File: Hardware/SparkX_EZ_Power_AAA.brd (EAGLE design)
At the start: 10.7 x 40.6 mm, 43 parts, among them J3 AVR_SPI_PROG_3X2TESTPOINTS, U1 ATTINY43_QFN20, U2 TPS61200

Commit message: Post-review updates
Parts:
- added RXD, TXD: TEST-POINT3X4, SparkFun-Connectors:PAD.03X.04
- added U$4: (no value), output:#TXD#0
- added U$9: (no value), output:#RXD#0
- C1: device SparkFun-Capacitors:0603 -> SparkFun-Capacitors:0402-TIGHT
- C2, C4, C6: device SparkFun-Capacitors:0402 -> SparkFun-Capacitors:0402-TIGHT
- L2: device SparkFun:CDRH2D09 -> SparkFun-Coils:1008(2520)
- R1, R2, R3: device SparkFun-Resistors:0603 -> New-Parts_SparkFun-Resistors:0402-TIGHT
- U2: device SparkFun:QFN-10_PAD -> SparkFun-IC-Power:QFN-10_PAD
- moved U$5 5.12 mm to (8.95, 34.5)
- moved U$2 3.43 mm to (9.84, 11.7)
- moved R1 3.23 mm to (2.35, 8.19)
- moved VIN 2.84 mm to (7.62, 35.6)
- moved R2 2.29 mm to (8.83, 9.78)
- moved U$20 1.27 mm to (5.33, 27.9)
- moved U$3 0.64 mm to (5.33, 26.0)
- moved L2 0.64 mm to (5.84, 9.78)
- moved R3 0.54 mm to (4.76, 17.0)
- moved C6 0.34 mm to (2.35, 11.4)
- moved C4 0.32 mm to (2.35, 12.5)
- moved C2 0.32 mm to (6.92, 17.5)
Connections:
- new net RXD: RXD.1, U1.16
- new net TXD: TXD.1, U1.15
- net N$1: now also L2.1; no longer L2.P$1
- net VIN: now also L2.2; no longer L2.P$2
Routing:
- net VIN: track 57.7 -> 47.2 mm
- net TXD: track 0.00 -> 8.27 mm, vias 0 -> 1
- net RXD: track 0.00 -> 2.65 mm, vias 0 -> 1
- net 3.3V: track 70.9 -> 71.9 mm
- net UVLO: track 4.30 -> 3.74 mm
- net GND: track 85.3 -> 85.0 mm, vias 44 -> 46
- net FB: track 15.9 -> 15.7 mm, vias 2 -> 3

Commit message: Post-review updates
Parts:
- L2: value 4.7uH, 1.2A -> 4.7μH; device SparkFun-Coils:1008(2520) -> SparkFun-Coils:INDUCTOR_4X4MM
- moved VIN 25.4 mm to (7.62, 10.2)
- moved U$5 24.6 mm to (5.40, 10.2)
- moved R2 6.36 mm to (2.98, 7.27), turned to 0 degrees
- moved U$4 4.76 mm to (3.94, 33.0)
- moved U$9 4.76 mm to (4.00, 30.5)
- moved U$2 2.67 mm to (9.65, 9.02)
- moved LOGO2 1.72 mm to (1.84, 16.7)
- moved L2 0.86 mm to (6.35, 9.08), turned to 90 degrees
- moved R1 0.64 mm to (2.98, 8.26)
- moved C3 0.32 mm to (2.32, 10.1)
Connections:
- net N$1: now also L2.P$1; no longer L2.1
- net VIN: now also L2.P$2; no longer L2.2
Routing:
- net FB: track 15.7 -> 9.68 mm, vias 3 -> 2
- net GND: track 85.0 -> 86.6 mm, vias 46 -> 47
- net VIN: track 47.2 -> 46.2 mm
- net N$1: track 3.09 -> 3.75 mm

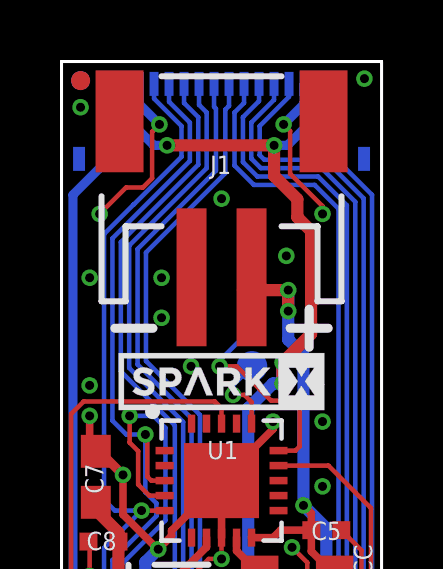
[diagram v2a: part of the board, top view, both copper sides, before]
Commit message: Add VIN Max 5.5V
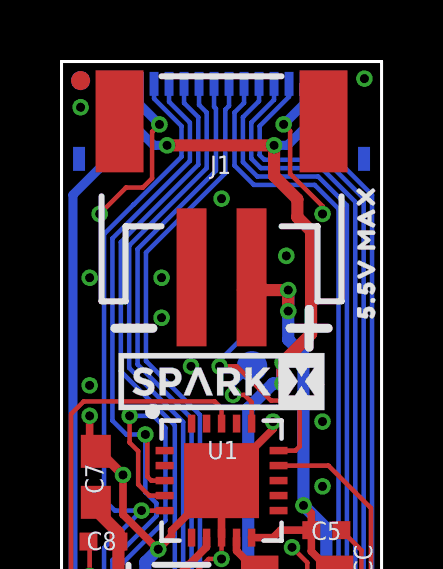
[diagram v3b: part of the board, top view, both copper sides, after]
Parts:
- added U$10: (no value), output:5#5V_MAX0
- U1: device New-Parts_SparkFun-IC-Microcontroller:QFN20_20M1 -> SparkFun-IC-Microcontroller:QFN20_20M1
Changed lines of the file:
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@@
 <element name="PROC_PWR_EN" library="SparkFun-Jumpers" package="SMT-JUMPER_2_NC_TRACE_SILK" package3d_urn="urn:adsk.eagle:package:39281/1" value="JUMPER-SMT_2_NC_TRACE_SILK" x="9.3345" y="3.6195" smashed="yes" rot="MR90"/>
 <element name="3V3_EN" library="SparkFun-Connectors" package="PAD.03X.04" value="TEST-POINT3X4" x="7.62" y="13.97" smashed="yes" rot="MR0"/>
-<element name="U1" library="New-Parts_SparkFun-IC-Microcontroller" package="QFN20_20M1" value="ATTINY43_QFN20" x="5.334" y="26.67" smashed="yes">
+<element name="U1" library="SparkFun-IC-Microcontroller" package="QFN20_20M1" value="ATTINY43_QFN20" x="5.334" y="26.67" smashed="yes">
 <attribute name="DIGIKEY_PART" value="ATTINY43U-MU-ND" x="5.334" y="26.67" size="1.778" layer="27" font="vector" ratio="15" display="off"/>
 <attribute name="MANU_PART" value="ATtiny43U-MU" x="5.334" y="26.67" size="1.778" layer="27" font="vector" ratio="15" display="off"/>
@@
 <element name="U$4" library="output" package="#TXD#0" value="" x="3.937" y="33.02" smashed="yes" rot="MR0"/>
 <element name="U$9" library="output" package="#RXD#0" value="" x="4.0005" y="30.48" smashed="yes" rot="MR0"/>
+<element name="U$10" library="output" package="5#5V_MAX0" value="" x="10.16" y="34.29" smashed="yes" rot="R90"/>
 </elements>
 <signals>

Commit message: Final tweaks
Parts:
- added U$11: (no value), output:MAX0
- U$10: device output:5#5V_MAX0 -> output:5#5V0
- moved U$1 21.7 mm to (9.53, 8.64), turned to 90 degrees
- moved U$2 11.8 mm to (1.46, 17.5)
- moved LOGO2 7.51 mm to (9.33, 16.1), turned to 90 degrees
- moved U$10 4.06 mm to (8.95, 30.4), turned to 0 degrees
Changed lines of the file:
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@@
 <attribute name="PROD_ID" value="" x="5.334" y="2.0955" size="1.778" layer="27" font="vector" ratio="15" rot="R180" display="off"/>
 </element>
-<element name="LOGO2" library="SparkFun-Aesthetics" package="OSHW-LOGO-MINI" value="OSHW-LOGOMINI" x="1.8415" y="16.7005" smashed="yes"/>
-<element name="U$1" library="SparkX" package="SPARKX-SMALL" value="SPARKX-LOGO3" x="5.334" y="29.972" smashed="yes"/>
+<element name="LOGO2" library="SparkFun-Aesthetics" package="OSHW-LOGO-MINI" value="OSHW-LOGOMINI" x="9.3345" y="16.129" smashed="yes" rot="R90"/>
+<element name="U$1" library="SparkX" package="SPARKX-SMALL" value="SPARKX-LOGO3" x="9.525" y="8.636" smashed="yes" rot="R90"/>
 <element name="U$13" library="output" package="#OUT#0" value="" x="5.334" y="4.8895" smashed="yes"/>
 <element name="U$20" library="SparkX" package="SPARKX-SMALL" value="SPARKX-LOGO3" x="5.334" y="27.94" smashed="yes" rot="MR0"/>
@@
 <attribute name="PROD_ID" value="RES-15093" x="6.9215" y="16.4465" size="1.778" layer="27" ratio="15" rot="R180" display="off"/>
 </element>
-<element name="U$2" library="output" package="EZ_POWER_AAA0" value="" x="9.652" y="9.017" smashed="yes" rot="R90"/>
+<element name="U$2" library="output" package="EZ_POWER_AAA0" value="" x="1.4605" y="17.4625" smashed="yes" rot="R90"/>
 <element name="U$3" library="output" package="EZ_POWER_AAA0" value="" x="5.334" y="26.035" smashed="yes" rot="MR0"/>
 <element name="U2" library="SparkFun-IC-Power" package="QFN-10_PAD" value="TPS61200" x="5.334" y="13.97" smashed="yes">
@@
 <element name="U$4" library="output" package="#TXD#0" value="" x="3.937" y="33.02" smashed="yes" rot="MR0"/>
 <element name="U$9" library="output" package="#RXD#0" value="" x="4.0005" y="30.48" smashed="yes" rot="MR0"/>
-<element name="U$10" library="output" package="5#5V_MAX0" value="" x="10.16" y="34.29" smashed="yes" rot="R90"/>
+<element name="U$10" library="output" package="5#5V0" value="" x="8.9535" y="30.4165" smashed="yes"/>
+<element name="U$11" library="output" package="MAX0" value="" x="8.9535" y="29.464" smashed="yes"/>
 </elements>
 <signals>

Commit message: Gapless production panel
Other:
- board text added: "2-Layer Board 1.6mm Thickness 1oz Copper (Outer layers) HASL Finish"
- board text removed: "2-Layer Board 1.6mm Thickness 1oz Copper (Outer layers) HASL Finish When running the panelizer, add a vertical gap of 0.2" to make the boards easier to separate"
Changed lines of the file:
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@@
 <layer number="23" name="tOrigins" color="15" fill="1" visible="yes" active="yes"/>
 <layer number="24" name="bOrigins" color="15" fill="1" visible="yes" active="yes"/>
-<layer number="25" name="tNames" color="57" fill="1" visible="yes" active="yes"/>
-<layer number="26" name="bNames" color="57" fill="1" visible="yes" active="yes"/>
-<layer number="27" name="tValues" color="7" fill="1" visible="yes" active="yes"/>
-<layer number="28" name="bValues" color="7" fill="1" visible="yes" active="yes"/>
-<layer number="29" name="tStop" color="7" fill="3" visible="yes" active="yes"/>
-<layer number="30" name="bStop" color="7" fill="6" visible="yes" active="yes"/>
-<layer number="31" name="tCream" color="7" fill="4" visible="yes" active="yes"/>
-<layer number="32" name="bCream" color="7" fill="5" visible="yes" active="yes"/>
-<layer number="33" name="tFinish" color="6" fill="3" visible="yes" active="yes"/>
-<layer number="34" name="bFinish" color="6" fill="6" visible="yes" active="yes"/>
-<layer number="35" name="tGlue" color="7" fill="4" visible="yes" active="yes"/>
-<layer number="36" name="bGlue" color="7" fill="5" visible="yes" active="yes"/>
-<layer number="37" name="tTest" color="7" fill="1" visible="yes" active="yes"/>
-<layer number="38" name="bTest" color="7" fill="1" visible="yes" active="yes"/>
-<layer number="39" name="tKeepout" color="4" fill="11" visible="yes" active="yes"/>
-<layer number="40" name="bKeepout" color="1" fill="11" visible="yes" active="yes"/>
-<layer number="41" name="tRestrict" color="4" fill="10" visible="yes" active="yes"/>
-<layer number="42" name="bRestrict" color="1" fill="10" visible="yes" active="yes"/>
-<layer number="43" name="vRestrict" color="2" fill="10" visible="yes" active="yes"/>
-<layer number="44" name="Drills" color="7" fill="1" visible="yes" active="yes"/>
+<layer number="25" name="tNames" color="57" fill="1" visible="no" active="yes"/>
+<layer number="26" name="bNames" color="57" fill="1" visible="no" active="yes"/>
+<layer number="27" name="tValues" color="7" fill="1" visible="no" active="yes"/>
+<layer number="28" name="bValues" color="7" fill="1" visible="no" active="yes"/>
+<layer number="29" name="tStop" color="7" fill="3" visible="no" active="yes"/>
+<layer number="30" name="bStop" color="7" fill="6" visible="no" active="yes"/>
+<layer number="31" name="tCream" color="7" fill="4" visible="no" active="yes"/>
+<layer number="32" name="bCream" color="7" fill="5" visible="no" active="yes"/>
+<layer number="33" name="tFinish" color="6" fill="3" visible="no" active="yes"/>
+<layer number="34" name="bFinish" color="6" fill="6" visible="no" active="yes"/>
+<layer number="35" name="tGlue" color="7" fill="4" visible="no" active="yes"/>
+<layer number="36" name="bGlue" color="7" fill="5" visible="no" active="yes"/>
+<layer number="37" name="tTest" color="7" fill="1" visible="no" active="yes"/>
+<layer number="38" name="bTest" color="7" fill="1" visible="no" active="yes"/>
+<layer number="39" name="tKeepout" color="4" fill="11" visible="no" active="yes"/>
+<layer number="40" name="bKeepout" color="1" fill="11" visible="no" active="yes"/>
+<layer number="41" name="tRestrict" color="4" fill="10" visible="no" active="yes"/>
+<layer number="42" name="bRestrict" color="1" fill="10" visible="no" active="yes"/>
+<layer number="43" name="vRestrict" color="2" fill="10" visible="no" active="yes"/>
+<layer number="44" name="Drills" color="7" fill="1" visible="no" active="yes"/>
 <layer number="45" name="Holes" color="7" fill="1" visible="yes" active="yes"/>
-<layer number="46" name="Milling" color="3" fill="1" visible="yes" active="yes"/>
-<layer number="47" name="Measures" color="7" fill="1" visible="yes" active="yes"/>
-<layer number="48" name="Document" color="7" fill="1" visible="yes" active="yes"/>
-<layer number="49" name="Reference" color="7" fill="1" visible="yes" active="yes"/>
-<layer number="50" name="dxf" color="7" fill="1" visible="yes" active="yes"/>
+<layer number="46" name="Milling" color="3" fill="1" visible="no" active="yes"/>
+<layer number="47" name="Measures" color="7" fill="1" visible="no" active="yes"/>
+<layer number="48" name="Document" color="7" fill="1" visible="no" active="yes"/>
+<layer number="49" name="Reference" color="7" fill="1" visible="no" active="yes"/>
+<layer number="50" name="dxf" color="7" fill="1" visible="no" active="yes"/>
 <layer number="51" name="tDocu" color="6" fill="1" visible="yes" active="yes"/>
-<layer number="52" name="bDocu" color="7" fill="1" visible="yes" active="yes"/>
+<layer number="52" name="bDocu" color="7" fill="1" visible="no" active="yes"/>
 <layer number="2" name="Route2" color="63" fill="1" visible="no" active="no"/>
 <layer number="15" name="Route15" color="23" fill="1" visible="no" active="no"/>
@@
 1oz Copper (Outer layers)
 HASL Finish
-When running the panelizer, add a vertical gap of 0.2"
-to make the boards easier to separate</text>
+</text>
 <dimension x1="0" y1="0" x2="10.668" y2="0" x3="5.334" y3="-3.81" textsize="1.778" textratio="15" layer="47" dtype="horizontal" unit="inch"/>
 <dimension x1="0" y1="40.64" x2="0" y2="0" x3="-6.350003125" y3="20.32" textsize="1.778" textratio="15" layer="47" dtype="vertical" unit="inch"/>

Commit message: Update 16-way FPC Connector. Add missing PROD_IDs
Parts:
- IN, OUT: value FPC_16_0.5MM_BACKFLIP -> (none); device New_Parts_Connectors:FPC_16_DOUBLESIDED_BACKFLIP -> SparkFun-Connectors:FPC_16_0.5MM
- R1, R2, R3: device New-Parts_SparkFun-Resistors:0402-TIGHT -> SparkFun-Resistors:0402-TIGHT
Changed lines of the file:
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@@
 <element name="FD3" library="SparkFun-Aesthetics" package="FIDUCIAL-MICRO" value="FIDUCIALUFIDUCIAL" x="10.033" y="0.635" smashed="yes"/>
 <element name="FD4" library="SparkFun-Aesthetics" package="FIDUCIAL-MICRO" value="FIDUCIALUFIDUCIAL" x="10.033" y="0.635" smashed="yes" rot="MR0"/>
-<element name="OUT" library="New_Parts_Connectors" package="FPC_16_DOUBLESIDED_BACKFLIP" value="FPC_16_0.5MM_BACKFLIP" x="5.334" y="2.0955" smashed="yes" rot="R180">
-<attribute name="ATOM_PART" value="FPC05016-42201" x="5.334" y="2.0955" size="1.778" layer="27" font="vector" ratio="15" rot="R180" display="off"/>
-<attribute name="PROD_ID" value="" x="5.334" y="2.0955" size="1.778" layer="27" font="vector" ratio="15" rot="R180" display="off"/>
+<element name="OUT" library="SparkFun-Connectors" package="FPC_16_0.5MM" value="" x="5.334" y="2.0955" smashed="yes" rot="R180">
+<attribute name="PROD_ID" value="CONN-16066" x="5.334" y="2.0955" size="1.778" layer="27" font="vector" ratio="15" rot="R180" display="off"/>
 </element>
 <element name="LOGO2" library="SparkFun-Aesthetics" package="OSHW-LOGO-MINI" value="OSHW-LOGOMINI" x="9.3345" y="16.129" smashed="yes" rot="R90"/>
@@
 <element name="U$20" library="SparkX" package="SPARKX-SMALL" value="SPARKX-LOGO3" x="5.334" y="27.94" smashed="yes" rot="MR0"/>
 <element name="LOGO3" library="SparkFun-Aesthetics" package="OSHW-LOGO-MINI" value="OSHW-LOGOMINI" x="5.334" y="23.495" smashed="yes" rot="MR0"/>
-<element name="IN" library="New_Parts_Connectors" package="FPC_16_DOUBLESIDED_BACKFLIP" value="FPC_16_0.5MM_BACKFLIP" x="5.334" y="38.5445" smashed="yes" rot="MR0">
-<attribute name="ATOM_PART" value="FPC05016-42201" x="5.334" y="38.5445" size="1.778" layer="28" ratio="15" rot="MR0" display="off"/>
-<attribute name="PROD_ID" value="" x="5.334" y="38.5445" size="1.778" layer="28" ratio="15" rot="MR0" display="off"/>
+<element name="IN" library="SparkFun-Connectors" package="FPC_16_0.5MM" value="" x="5.334" y="38.5445" smashed="yes" rot="MR0">
+<attribute name="PROD_ID" value="CONN-16066" x="5.334" y="38.5445" size="1.778" layer="28" ratio="15" rot="MR0" display="off"/>
 </element>
 <element name="U$12" library="output" package="#IN#0" value="" x="5.334" y="34.798" smashed="yes" rot="MR0"/>
@@
 <attribute name="MANU_PART" value="ATtiny43U-MU" x="5.334" y="26.67" size="1.778" layer="27" font="vector" ratio="15" display="off"/>
 <attribute name="NAME" x="4.858" y="27.384" size="0.6096" layer="25" ratio="20"/>
-<attribute name="PROD_ID" value="" x="5.334" y="26.67" size="1.778" layer="27" font="vector" ratio="15" display="off"/>
+<attribute name="PROD_ID" value="IC-16068" x="5.334" y="26.67" size="1.778" layer="27" font="vector" ratio="15" display="off"/>
 </element>
 <element name="C5" library="SparkFun-Capacitors" package="0402-TIGHT" value="4.7uF" x="8.8265" y="25.019" smashed="yes">
@@
 <attribute name="PROD_ID" value="CAP-14993" x="2.3495" y="12.5095" size="1.778" layer="27" rot="R180" display="off"/>
 </element>
-<element name="R3" library="New-Parts_SparkFun-Resistors" package="0402-TIGHT" value="453k" x="4.7625" y="16.9545" smashed="yes" rot="R180">
+<element name="R3" library="SparkFun-Resistors" package="0402-TIGHT" value="453k" x="4.7625" y="16.9545" smashed="yes" rot="R180">
 <attribute name="NAME" x="5.207" y="17.272" size="0.6096" layer="25" font="vector" ratio="20" rot="R180"/>
-<attribute name="PROD_ID" value="" x="4.7625" y="16.9545" size="1.778" layer="27" rot="R180" display="off"/>
+<attribute name="PROD_ID" value="RES-15345" x="4.7625" y="16.9545" size="1.778" layer="27" rot="R180" display="off"/>
 </element>
-<element name="R1" library="New-Parts_SparkFun-Resistors" package="0402-TIGHT" value="1M" x="2.9845" y="8.255" smashed="yes" rot="R180">
+<element name="R1" library="SparkFun-Resistors" package="0402-TIGHT" value="1M" x="2.9845" y="8.255" smashed="yes" rot="R180">
 <attribute name="NAME" x="3.429" y="8.509" size="0.6096" layer="25" font="vector" ratio="20" rot="R180"/>
-<attribute name="PROD_ID" value="" x="2.9845" y="8.255" size="1.778" layer="27" rot="R180" display="off"/>
+<attribute name="PROD_ID" value="RES-15185" x="2.9845" y="8.255" size="1.778" layer="27" rot="R180" display="off"/>
 </element>
-<element name="R2" library="New-Parts_SparkFun-Resistors" package="0402-TIGHT" value="180k" x="2.9845" y="7.27075" smashed="yes">
+<element name="R2" library="SparkFun-Resistors" package="0402-TIGHT" value="180k" x="2.9845" y="7.27075" smashed="yes">
 <attribute name="NAME" x="2.54" y="6.95325" size="0.6096" layer="25" font="vector" ratio="20"/>
-<attribute name="PROD_ID" value="" x="2.9845" y="7.27075" size="1.778" layer="27" display="off"/>
+<attribute name="PROD_ID" value="RES-16069" x="2.9845" y="7.27075" size="1.778" layer="27" display="off"/>
 <attribute name="VALUE" value="180k" x="2.9845" y="7.27075" size="1.778" layer="27" display="off"/>
 </element>
